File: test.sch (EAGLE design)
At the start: 14 parts

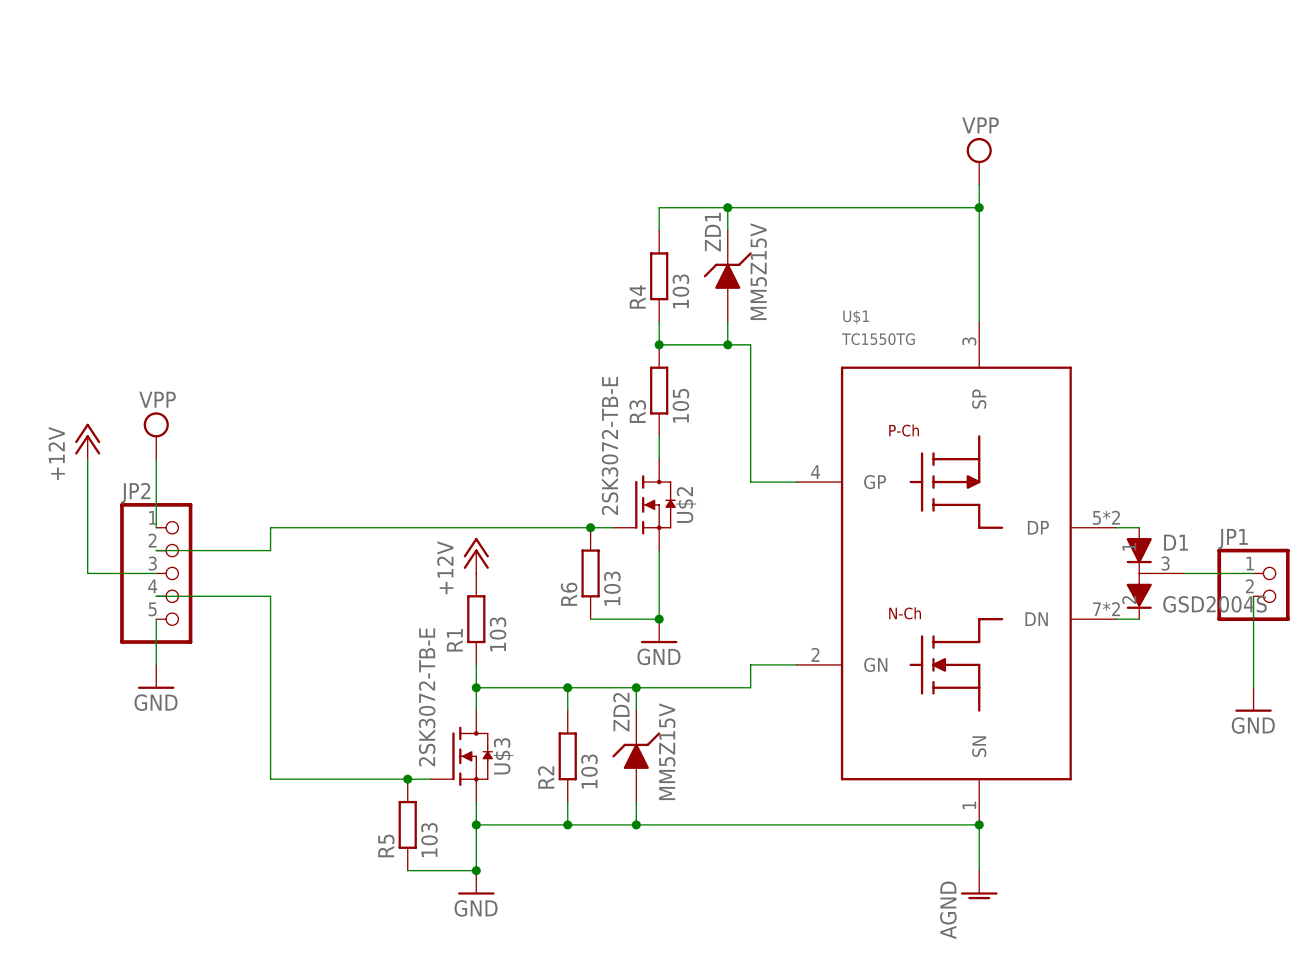
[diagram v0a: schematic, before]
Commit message: added a NPN for like voltage follower
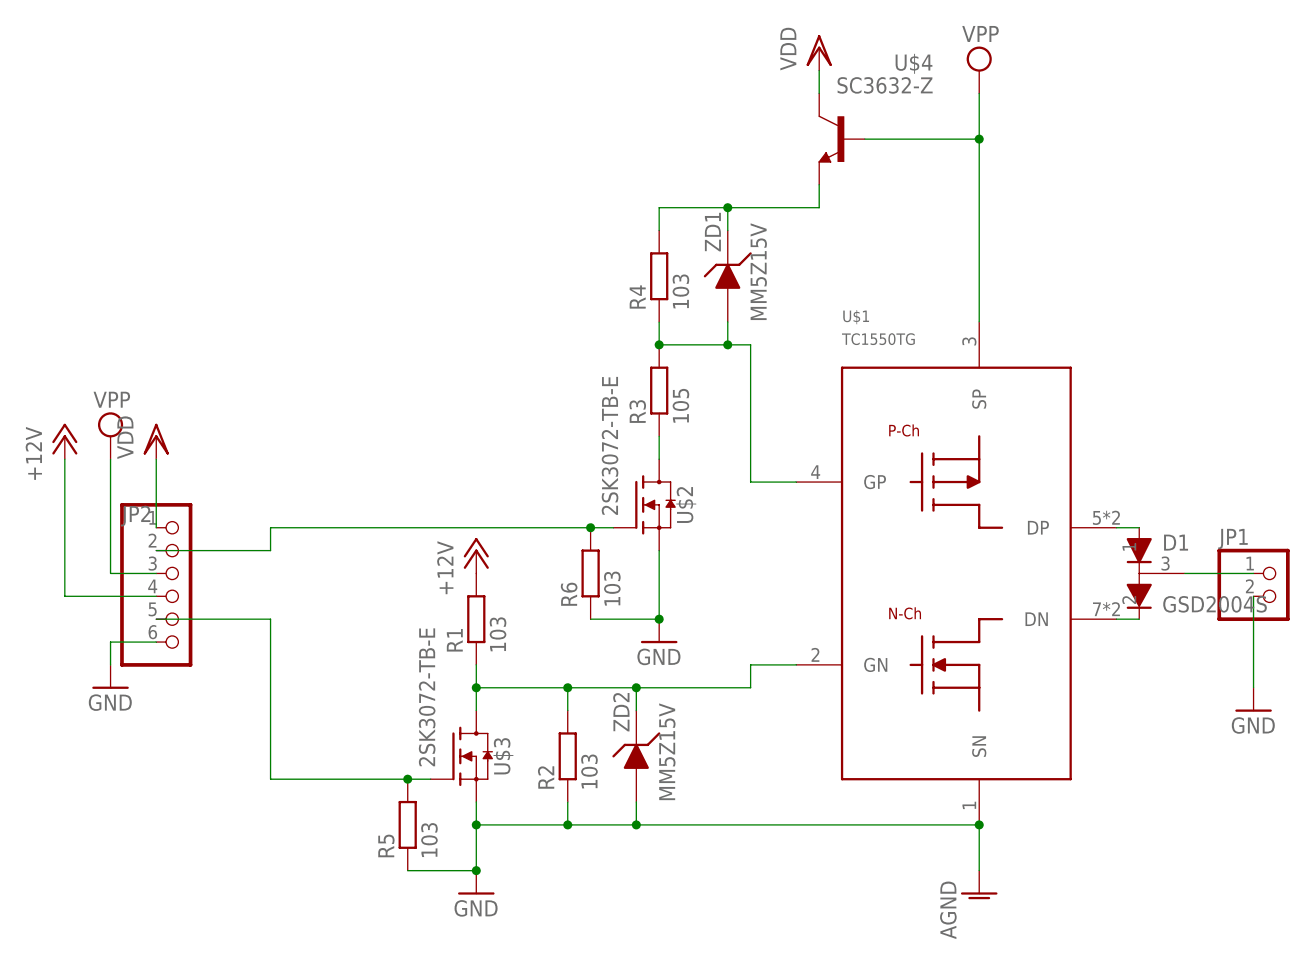
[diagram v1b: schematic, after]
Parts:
- added U$4: SC3632-Z, Transistor-NPN:SC3632-Z
- JP2: device pinhead:PINHD-1X5 -> pinhead:PINHD-1X6
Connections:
- new net N$6: R4.2, U$4.E, ZD1.K
- new net VDD: JP2.1, U$4.C
- net +12V: now also JP2.4; no longer JP2.3
- net GND: now also JP2.6; no longer JP2.5
- net N$4: now also JP2.5; no longer JP2.4
- net VPP: now also JP2.3, U$4.B; no longer JP2.1, R4.2, ZD1.K
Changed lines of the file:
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@@
 <?xml version="1.0" encoding="utf-8"?>
 <!DOCTYPE eagle SYSTEM "eagle.dtd">
-<eagle version="9.3.2">
+<eagle version="9.4.2">
 <drawing>
 <settings>
@@
 <part name="R6" library="rcl" library_urn="urn:adsk.eagle:library:334" deviceset="R-EU_" device="0204/5" package3d_urn="urn:adsk.eagle:package:23488/1" value="103"/>
 <part name="JP1" library="pinhead" library_urn="urn:adsk.eagle:library:325" deviceset="PINHD-1X2" device="" package3d_urn="urn:adsk.eagle:package:22435/2"/>
-<part name="JP2" library="pinhead" library_urn="urn:adsk.eagle:library:325" deviceset="PINHD-1X5" device="" package3d_urn="urn:adsk.eagle:package:22469/2"/>
+<part name="JP2" library="pinhead" library_urn="urn:adsk.eagle:library:325" deviceset="PINHD-1X6" device="" package3d_urn="urn:adsk.eagle:package:22472/2"/>
 <part name="SUPPLY1" library="supply2" library_urn="urn:adsk.eagle:library:372" deviceset="VPP" device=""/>
 <part name="SUPPLY2" library="supply2" library_urn="urn:adsk.eagle:library:372" deviceset="VPP" device=""/>
@@
 <part name="D1" library="Diode_Vishay" library_urn="urn:adsk.eagle:library:10199852" deviceset="GSD2004S" device="" package3d_urn="urn:adsk.eagle:package:10199855/1"/>
 <part name="P+2" library="supply1" library_urn="urn:adsk.eagle:library:371" deviceset="+12V" device=""/>
+<part name="U$4" library="Transistor-NPN" library_urn="urn:adsk.eagle:library:11967480" deviceset="SC3632-Z" device="" package3d_urn="urn:adsk.eagle:package:11967296/2"/>
+<part name="VDD1" library="supply1" library_urn="urn:adsk.eagle:library:371" deviceset="VDD" device=""/>
+<part name="VDD2" library="supply1" library_urn="urn:adsk.eagle:library:371" deviceset="VDD" device=""/>
 </parts>
 <sheets>
@@
 <attribute name="VALUE" x="158.75" y="35.56" size="1.778" layer="96"/>
 </instance>
-<instance part="JP2" gate="A" x="43.18" y="43.18" smashed="yes">
-<attribute name="NAME" x="36.83" y="51.435" size="1.778" layer="95"/>
-<attribute name="VALUE" x="36.83" y="33.02" size="1.778" layer="96"/>
-</instance>
-<instance part="SUPPLY1" gate="G$1" x="132.08" y="88.9" smashed="yes">
-<attribute name="VALUE" x="130.175" y="92.075" size="1.778" layer="96"/>
-</instance>
-<instance part="SUPPLY2" gate="G$1" x="40.64" y="58.42" smashed="yes">
-<attribute name="VALUE" x="38.735" y="61.595" size="1.778" layer="96"/>
-</instance>
-<instance part="GND3" gate="1" x="40.64" y="30.48" smashed="yes">
-<attribute name="VALUE" x="38.1" y="27.94" size="1.778" layer="96"/>
+<instance part="JP2" gate="A" x="43.18" y="40.64" smashed="yes">
+<attribute name="NAME" x="36.83" y="48.895" size="1.778" layer="95"/>
+<attribute name="VALUE" x="36.83" y="30.48" size="1.778" layer="96"/>
+</instance>
+<instance part="SUPPLY1" gate="G$1" x="132.08" y="99.06" smashed="yes">
+<attribute name="VALUE" x="130.175" y="102.235" size="1.778" layer="96"/>
+</instance>
+<instance part="SUPPLY2" gate="G$1" x="35.56" y="58.42" smashed="yes">
+<attribute name="VALUE" x="33.655" y="61.595" size="1.778" layer="96"/>
+</instance>
+<instance part="GND3" gate="1" x="35.56" y="30.48" smashed="yes">
+<attribute name="VALUE" x="33.02" y="27.94" size="1.778" layer="96"/>
 </instance>
 <instance part="GND4" gate="1" x="162.56" y="27.94" smashed="yes">
@@
 <attribute name="VALUE" x="152.4" y="40.64" size="1.778" layer="96" align="top-left"/>
 </instance>
-<instance part="P+2" gate="1" x="33.02" y="58.42" smashed="yes">
-<attribute name="VALUE" x="30.48" y="53.34" size="1.778" layer="96" rot="R90"/>
+<instance part="P+2" gate="1" x="30.48" y="58.42" smashed="yes">
+<attribute name="VALUE" x="27.94" y="53.34" size="1.778" layer="96" rot="R90"/>
+</instance>
+<instance part="U$4" gate="G$1" x="116.84" y="91.44" smashed="yes" rot="MR0">
+<attribute name="NAME" x="127" y="99.06" size="1.778" layer="95" rot="MR0"/>
+<attribute name="VALUE" x="127" y="96.52" size="1.778" layer="96" rot="MR0"/>
+</instance>
+<instance part="VDD1" gate="G$1" x="114.3" y="101.6" smashed="yes">
+<attribute name="VALUE" x="111.76" y="99.06" size="1.778" layer="96" rot="R90"/>
+</instance>
+<instance part="VDD2" gate="G$1" x="40.64" y="58.42" smashed="yes">
+<attribute name="VALUE" x="38.1" y="55.88" size="1.778" layer="96" rot="R90"/>
 </instance>
 </instances>
@@
 <segment>
 <pinref part="P+2" gate="1" pin="+12V"/>
-<wire x1="33.02" y1="55.88" x2="33.02" y2="43.18" width="0.1524" layer="91"/>
-<pinref part="JP2" gate="A" pin="3"/>
-<wire x1="33.02" y1="43.18" x2="40.64" y2="43.18" width="0.1524" layer="91"/>
+<wire x1="30.48" y1="55.88" x2="30.48" y2="40.64" width="0.1524" layer="91"/>
+<pinref part="JP2" gate="A" pin="4"/>
+<wire x1="30.48" y1="40.64" x2="40.64" y2="40.64" width="0.1524" layer="91"/>
 </segment>
 </net>
@@
 </segment>
 <segment>
-<pinref part="JP2" gate="A" pin="5"/>
+<pinref part="JP2" gate="A" pin="6"/>
 <pinref part="GND3" gate="1" pin="GND"/>
-<wire x1="40.64" y1="38.1" x2="40.64" y2="33.02" width="0.1524" layer="91"/>
+<wire x1="40.64" y1="35.56" x2="35.56" y2="35.56" width="0.1524" layer="91"/>
+<wire x1="35.56" y1="35.56" x2="35.56" y2="33.02" width="0.1524" layer="91"/>
 </segment>
 </net>
@@
 <junction x="88.9" y="48.26"/>
 <pinref part="JP2" gate="A" pin="2"/>
+<wire x1="53.34" y1="45.72" x2="53.34" y2="48.26" width="0.1524" layer="91"/>
 <wire x1="40.64" y1="45.72" x2="53.34" y2="45.72" width="0.1524" layer="91"/>
-<wire x1="53.34" y1="45.72" x2="53.34" y2="48.26" width="0.1524" layer="91"/>
 </segment>
 </net>
@@
 <net name="VPP" class="0">
 <segment>
+<pinref part="U$1" gate="G$1" pin="SP"/>
+<wire x1="119.38" y1="91.44" x2="132.08" y2="91.44" width="0.1524" layer="91"/>
+<wire x1="132.08" y1="91.44" x2="132.08" y2="71.12" width="0.1524" layer="91"/>
+<pinref part="SUPPLY1" gate="G$1" pin="VPP"/>
+<wire x1="132.08" y1="96.52" x2="132.08" y2="91.44" width="0.1524" layer="91"/>
+<junction x="132.08" y="91.44"/>
+<pinref part="U$4" gate="G$1" pin="B"/>
+</segment>
+<segment>
 <pinref part="SUPPLY2" gate="G$1" pin="VPP"/>
-<pinref part="JP2" gate="A" pin="1"/>
-<wire x1="40.64" y1="55.88" x2="40.64" y2="48.26" width="0.1524" layer="91"/>
-</segment>
-<segment>
-<pinref part="R4" gate="G$1" pin="2"/>
-<wire x1="96.52" y1="81.28" x2="96.52" y2="83.82" width="0.1524" layer="91"/>
-<wire x1="96.52" y1="83.82" x2="104.14" y2="83.82" width="0.1524" layer="91"/>
-<pinref part="U$1" gate="G$1" pin="SP"/>
-<wire x1="104.14" y1="83.82" x2="132.08" y2="83.82" width="0.1524" layer="91"/>
-<wire x1="132.08" y1="83.82" x2="132.08" y2="71.12" width="0.1524" layer="91"/>
-<pinref part="ZD1" gate="G$1" pin="K"/>
-<wire x1="104.14" y1="81.28" x2="104.14" y2="83.82" width="0.1524" layer="91"/>
-<junction x="104.14" y="83.82"/>
-<pinref part="SUPPLY1" gate="G$1" pin="VPP"/>
-<wire x1="132.08" y1="86.36" x2="132.08" y2="83.82" width="0.1524" layer="91"/>
-<junction x="132.08" y="83.82"/>
+<wire x1="35.56" y1="55.88" x2="35.56" y2="43.18" width="0.1524" layer="91"/>
+<pinref part="JP2" gate="A" pin="3"/>
+<wire x1="35.56" y1="43.18" x2="40.64" y2="43.18" width="0.1524" layer="91"/>
 </segment>
 </net>
 <net name="N$4" class="0">
 <segment>
-<pinref part="JP2" gate="A" pin="4"/>
-<wire x1="40.64" y1="40.64" x2="53.34" y2="40.64" width="0.1524" layer="91"/>
 <pinref part="R5" gate="G$1" pin="2"/>
 <pinref part="U$3" gate="G$1" pin="G"/>
@@
 <wire x1="68.58" y1="20.32" x2="53.34" y2="20.32" width="0.1524" layer="91"/>
 <junction x="68.58" y="20.32"/>
-<wire x1="53.34" y1="40.64" x2="53.34" y2="20.32" width="0.1524" layer="91"/>
-</segment>
-</net>
+<pinref part="JP2" gate="A" pin="5"/>
+<wire x1="53.34" y1="38.1" x2="53.34" y2="20.32" width="0.1524" layer="91"/>
+<wire x1="40.64" y1="38.1" x2="53.34" y2="38.1" width="0.1524" layer="91"/>
+</segment>
+</net>
+<net name="N$6" class="0">
+<segment>
+<pinref part="ZD1" gate="G$1" pin="K"/>
+<wire x1="104.14" y1="81.28" x2="104.14" y2="83.82" width="0.1524" layer="91"/>
+<wire x1="96.52" y1="83.82" x2="104.14" y2="83.82" width="0.1524" layer="91"/>
+<pinref part="R4" gate="G$1" pin="2"/>
+<wire x1="96.52" y1="81.28" x2="96.52" y2="83.82" width="0.1524" layer="91"/>
+<wire x1="114.3" y1="83.82" x2="104.14" y2="83.82" width="0.1524" layer="91"/>
+<junction x="104.14" y="83.82"/>
+<wire x1="114.3" y1="86.36" x2="114.3" y2="83.82" width="0.1524" layer="91"/>
+<pinref part="U$4" gate="G$1" pin="E"/>
+</segment>
+</net>
+<net name="VDD" class="0">
+<segment>
+<pinref part="VDD1" gate="G$1" pin="VDD"/>
+<pinref part="U$4" gate="G$1" pin="C"/>
+<wire x1="114.3" y1="99.06" x2="114.3" y2="96.52" width="0.1524" layer="91"/>
+</segment>
+<segment>
+<pinref part="VDD2" gate="G$1" pin="VDD"/>
+<pinref part="JP2" gate="A" pin="1"/>
+<wire x1="40.64" y1="55.88" x2="40.64" y2="48.26" width="0.1524" layer="91"/>
+</segment>
+</net>

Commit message: replace the transistor with FET which compose a source follower.*
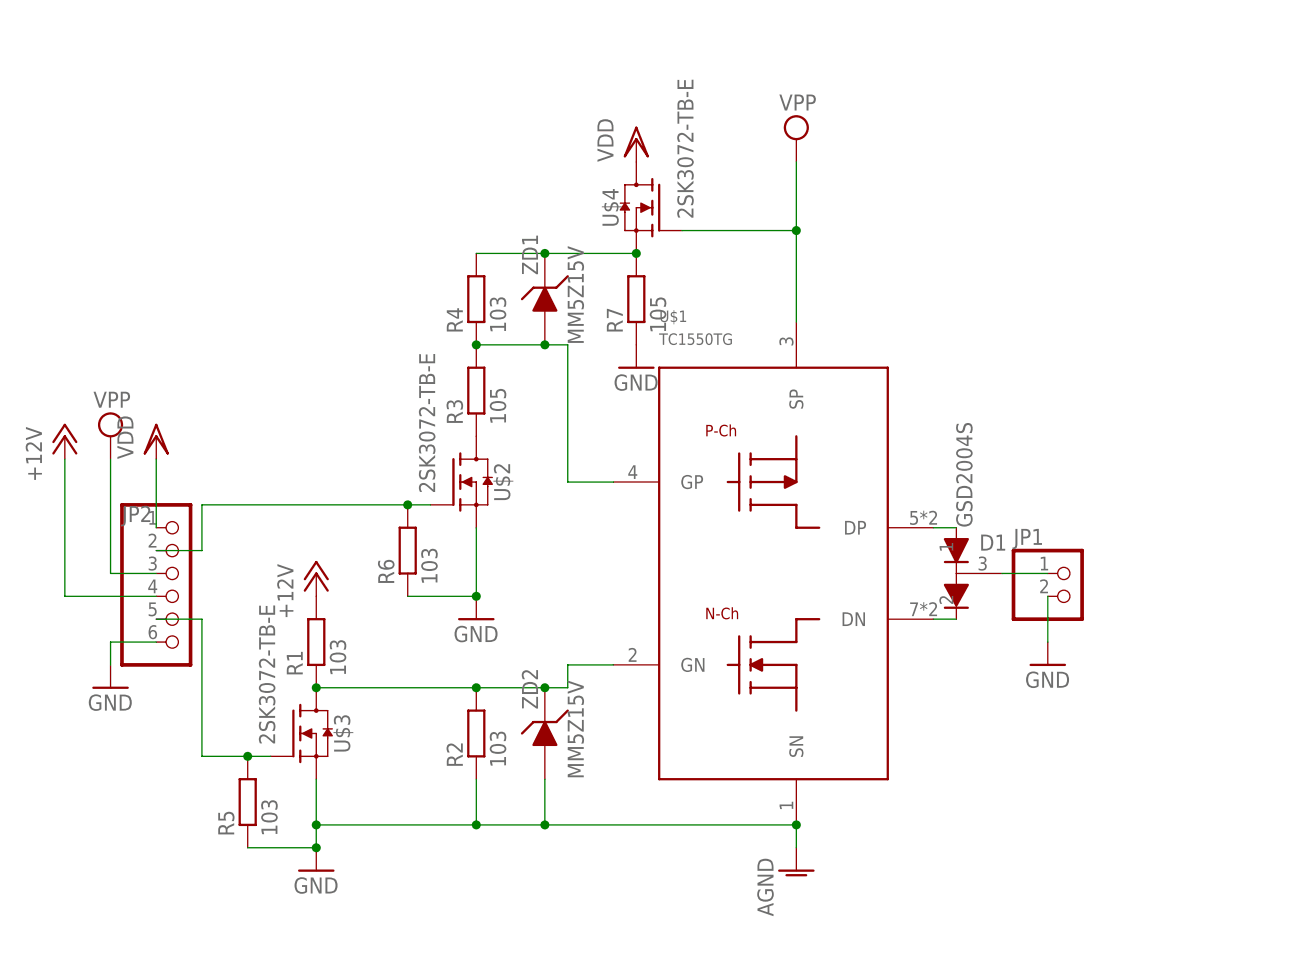
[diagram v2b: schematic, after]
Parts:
- added R7: 105, rcl:R-EU_0204/5
- U$4: value SC3632-Z -> 2SK3072-TB-E; device Transistor-NPN:SC3632-Z -> Transistor-FET:2SK3072-TB-E
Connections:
- net GND: now also R7.1
- net N$6: now also R7.2, U$4.S; no longer U$4.E
- net VDD: now also U$4.D; no longer U$4.C
- net VPP: now also U$4.G; no longer U$4.B
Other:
- moved on the sheet: D1, JP1, R1, R2, R3, R4, R5, R6, U$1, U$2, U$3, ZD1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

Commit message: rearrainged devies and added a solder junction
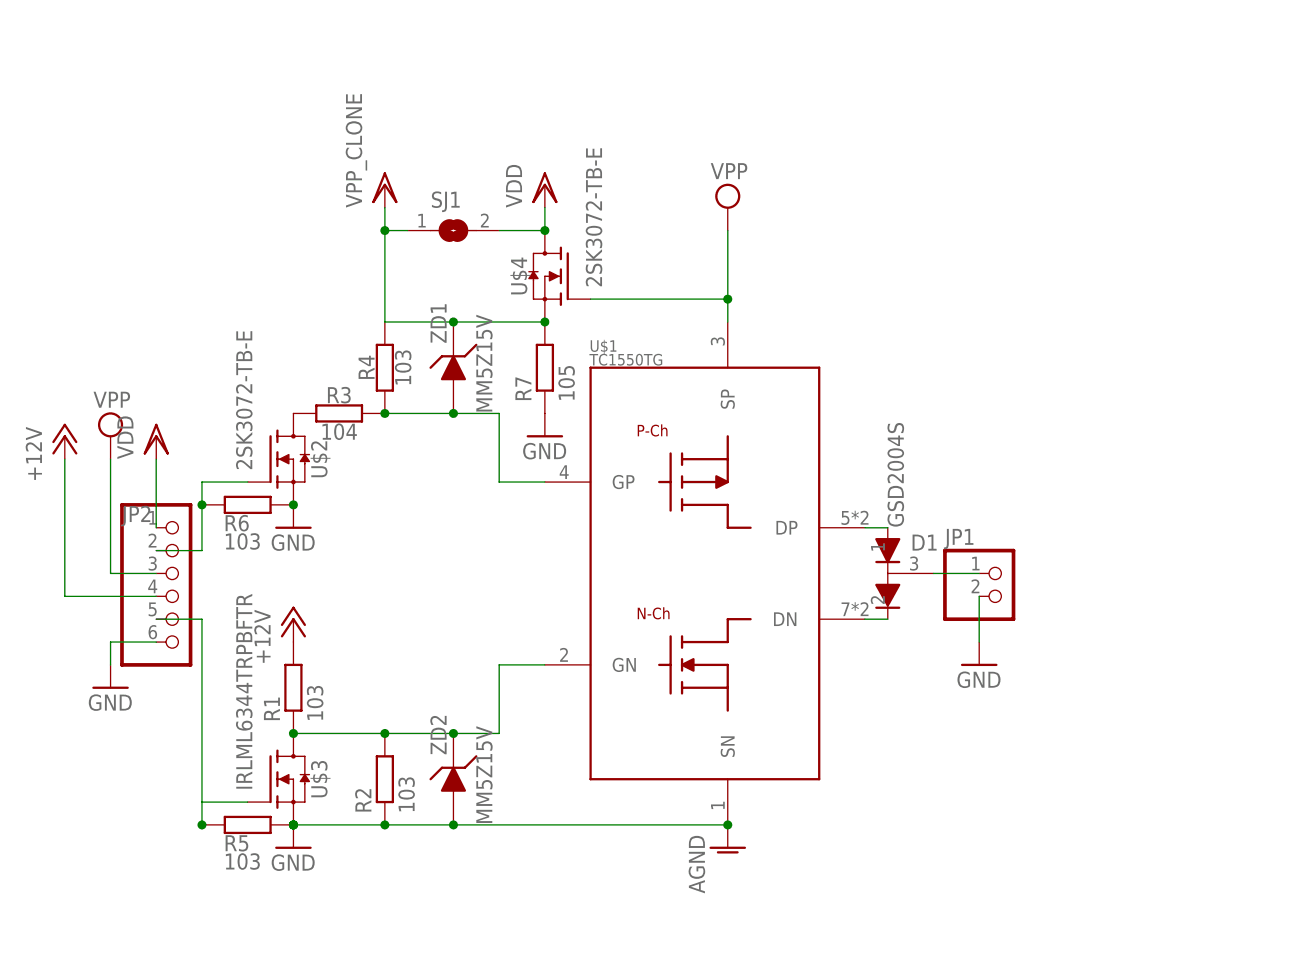
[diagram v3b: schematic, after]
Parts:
- added SJ1: (no value), jumper:SJ
- R3: value 105 -> 104
- U$3: value 2SK3072-TB-E -> IRLML6344TRPBFTR; device Transistor-FET:2SK3072-TB-E -> Transistor-FET:IRLML6344TRPBFTR
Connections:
- net N$6: now also SJ1.1
- net VDD: now also SJ1.2
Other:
- moved on the sheet: D1, JP1, R1, R2, R3, R4, R5, R6, R7, U$1, U$2, U$3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
